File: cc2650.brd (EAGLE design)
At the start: 50.8 x 22.9 mm, 23 parts, among them IC1 TPS73133DBVR, IC4 CC2650MODAMOHR, SW1 SPST_TACT-KMR2, SW3 SPST_TACT-KMR2

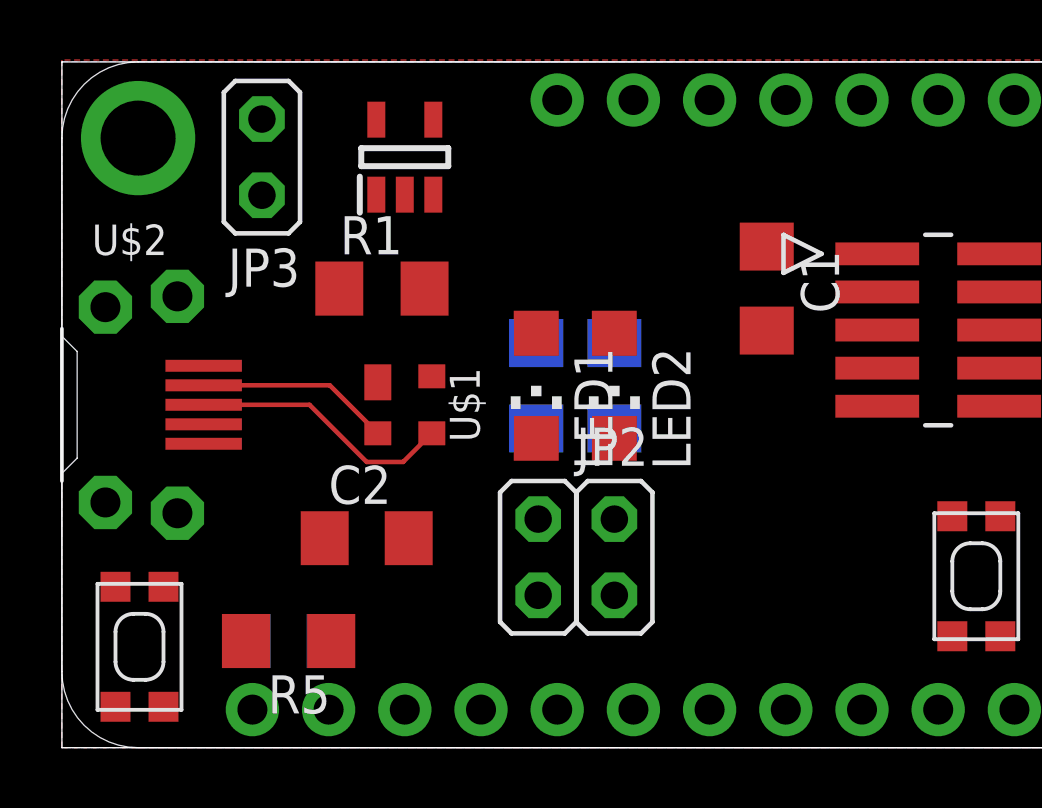
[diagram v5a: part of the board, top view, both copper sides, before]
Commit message: rearranged some components and hand routed some power signals.
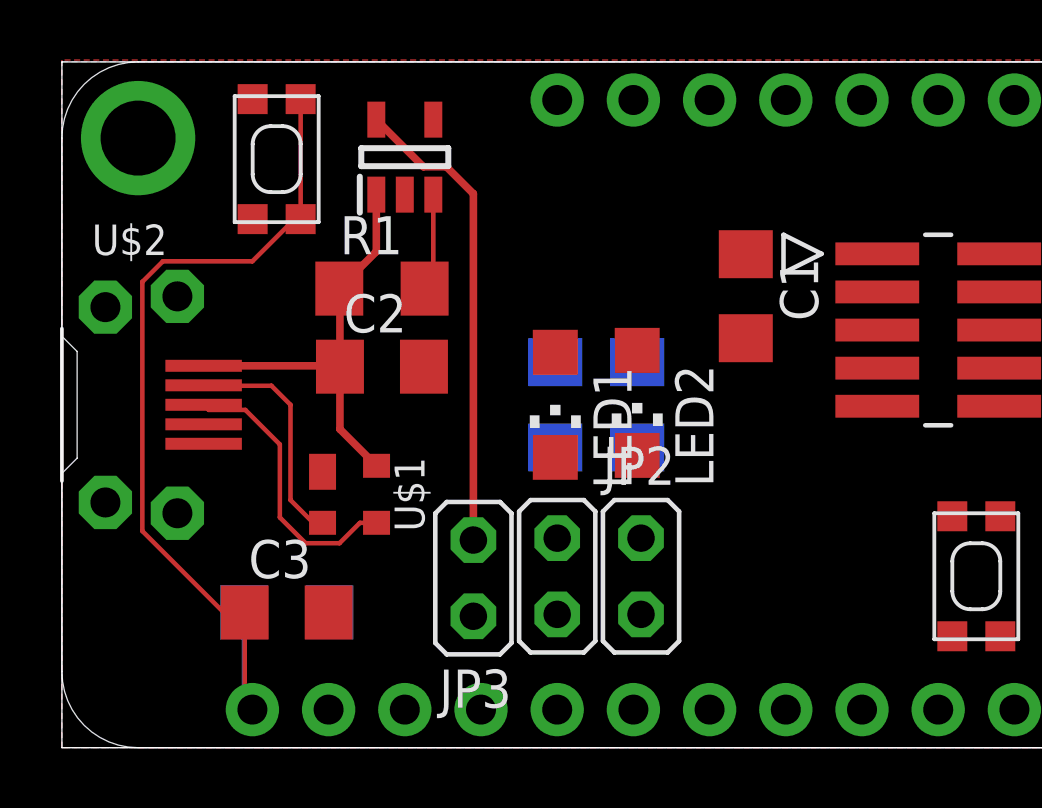
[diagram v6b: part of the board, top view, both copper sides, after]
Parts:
- moved SW1 16.9 mm to (7.16, 19.6)
- moved JP3 15.7 mm to (13.7, 5.65)
- moved C2 5.74 mm to (10.7, 12.7)
- moved U$1 3.51 mm to (9.59, 8.45)
- moved JP2 1.09 mm to (19.3, 5.71)
- moved R2 0.99 mm to (19.2, 11.4)
- moved C3 0.95 mm to (7.49, 4.51), flipped to the top, turned to 0 degrees
- moved R5 0.95 mm to (7.49, 4.51), flipped to the bottom, turned to 0 degrees
- moved LED2 0.95 mm to (19.2, 11.5)
- moved JP1 0.90 mm to (16.5, 5.71)
- moved LED1 0.90 mm to (16.4, 11.4)
- moved R3 0.90 mm to (16.4, 11.4)
- moved C1 0.74 mm to (22.8, 15.0)
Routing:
- net NRESET: track 0.00 -> 30.0 mm
- net N$5: track 0.00 -> 15.8 mm
- net VBUS: track 0.00 -> 14.6 mm
- net EN: track 0.00 -> 3.25 mm
- net D-: track 6.47 -> 7.72 mm
- net D+: track 8.79 -> 9.38 mm

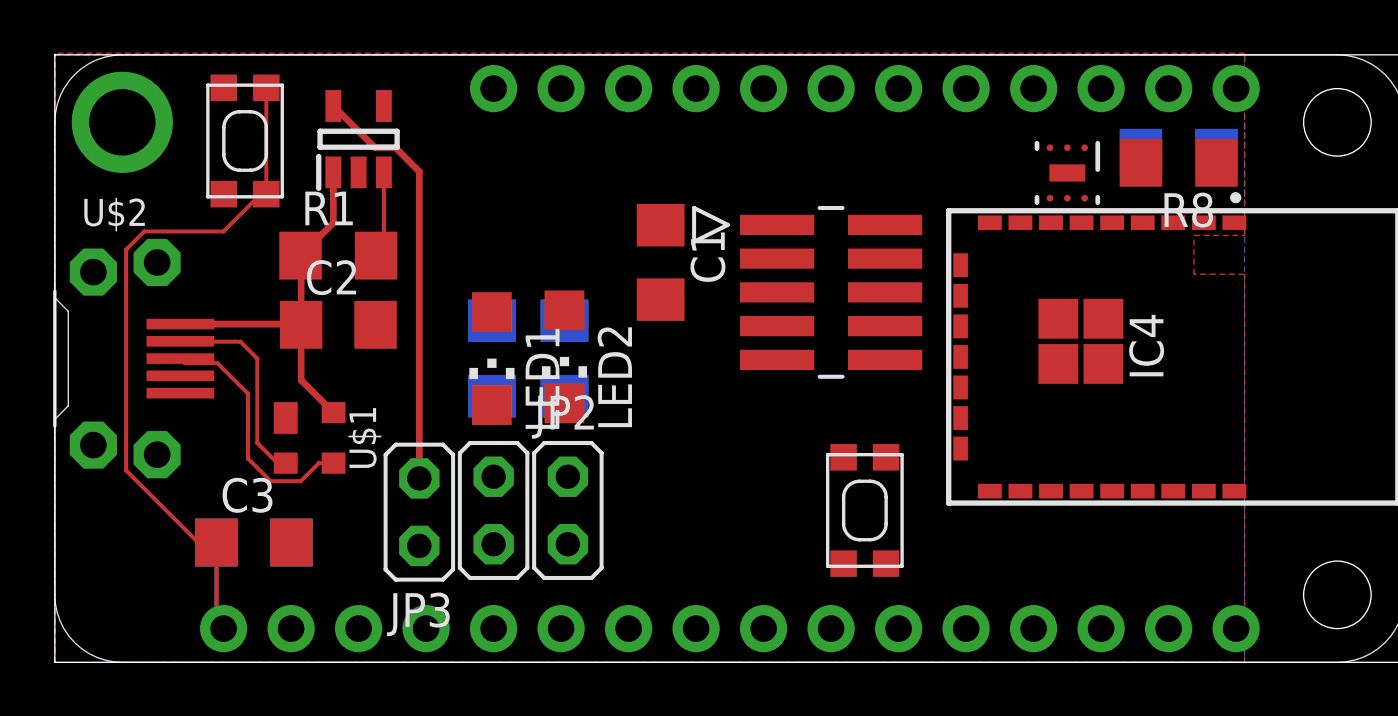
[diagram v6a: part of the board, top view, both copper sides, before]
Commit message: routed everything but light sensor
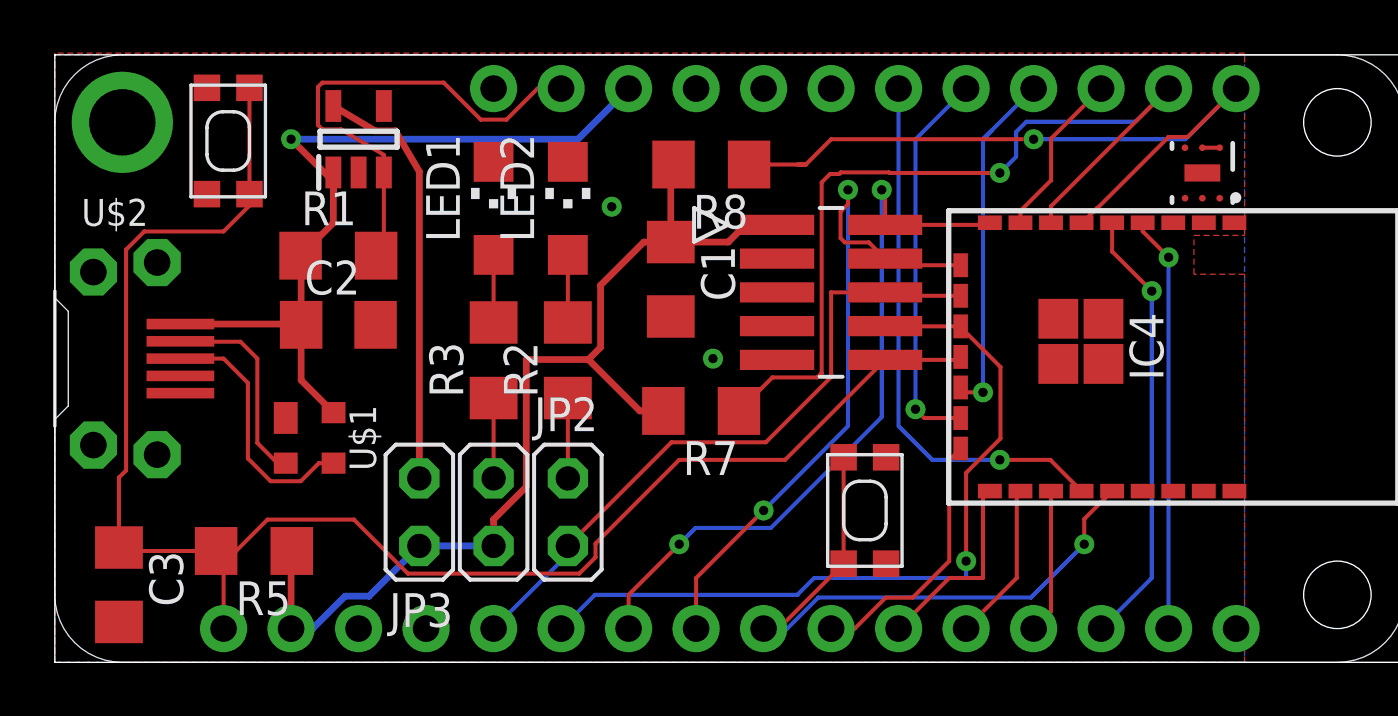
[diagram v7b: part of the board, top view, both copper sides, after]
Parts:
- moved R7 20.4 mm to (24.3, 9.46), flipped to the top, turned to 180 degrees
- moved R8 17.6 mm to (24.7, 18.7)
- moved LED1 5.65 mm to (16.5, 17.1), turned to 0 degrees
- moved LED2 5.59 mm to (19.3, 17.1), turned to 0 degrees
- moved C3 5.32 mm to (2.41, 2.92), turned to 270 degrees
- moved OPT3001 5.08 mm to (43.2, 18.4)
- moved C1 0.74 mm to (23.2, 14.4)
- moved SW1 0.63 mm to (6.52, 19.6)
- moved R5 0.32 mm to (7.49, 4.19), flipped to the top, turned to 180 degrees
- moved R2 0.14 mm to (19.3, 11.4), flipped to the top
- moved R3 0.09 mm to (16.5, 11.4), flipped to the top
- moved JP1 0.06 mm to (16.5, 5.65)
- moved JP2 0.06 mm to (19.3, 5.65)
- turned SW3 to 270 degrees
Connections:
- net N$1 renamed PWR_LED_JPR
- net N$2 renamed GPIO_LED
- net N$3 renamed GPIO_LED_JPR
- net N$32 renamed PWR_LED
- net N$5 renamed VCC_JPR
- removed net VBAT: MS1.28
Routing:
- net VCC: track 0.00 -> 39.5 mm
- net DIO3: track 0.00 -> 32.9 mm, vias 0 -> 1
- net NRESET: track 30.0 -> 62.1 mm
- net DIO6_TDI: track 0.00 -> 29.5 mm, vias 0 -> 1
- net DIO2: track 0.00 -> 27.9 mm, vias 0 -> 1
- net JTAG_TMS: track 0.00 -> 27.5 mm, vias 0 -> 2
- net JTAG_TCK: track 0.00 -> 25.7 mm, vias 0 -> 2
- net DIO5_TDO: track 0.00 -> 24.9 mm
- net DIO14: track 0.00 -> 23.8 mm, vias 0 -> 1
- net DIO13: track 0.00 -> 20.7 mm, vias 0 -> 1
- net DIO1_RX: track 0.00 -> 16.7 mm, vias 0 -> 1
- net VBUS: track 14.6 -> 30.7 mm, vias 0 -> 1
- net DIO0_TX: track 0.00 -> 15.7 mm, vias 0 -> 1
- net EN: track 3.25 -> 18.4 mm
- net DIO8: track 0.00 -> 14.7 mm, vias 0 -> 1
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
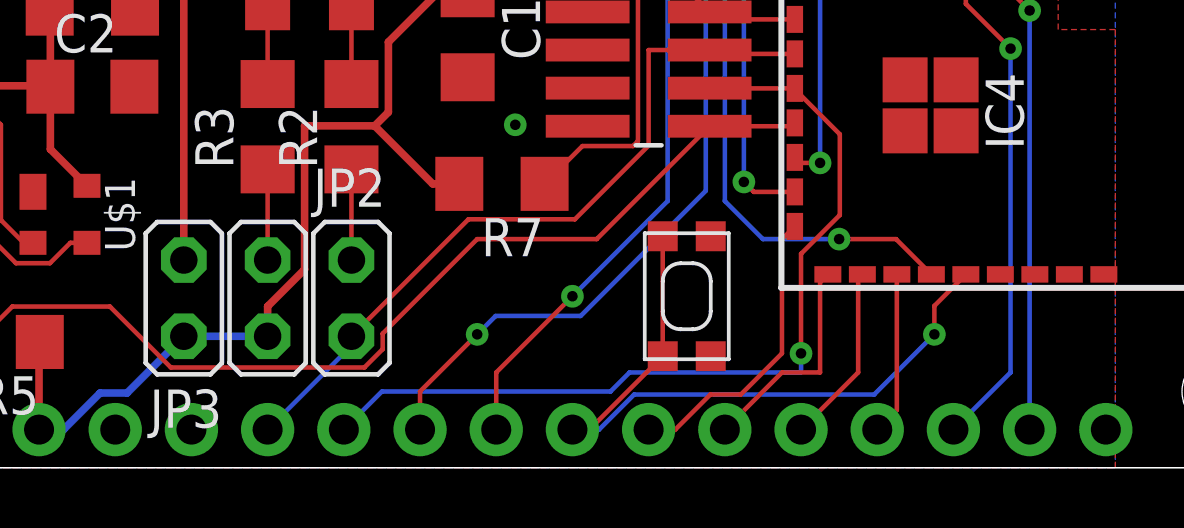
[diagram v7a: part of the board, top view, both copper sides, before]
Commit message: added one missed VCC connection
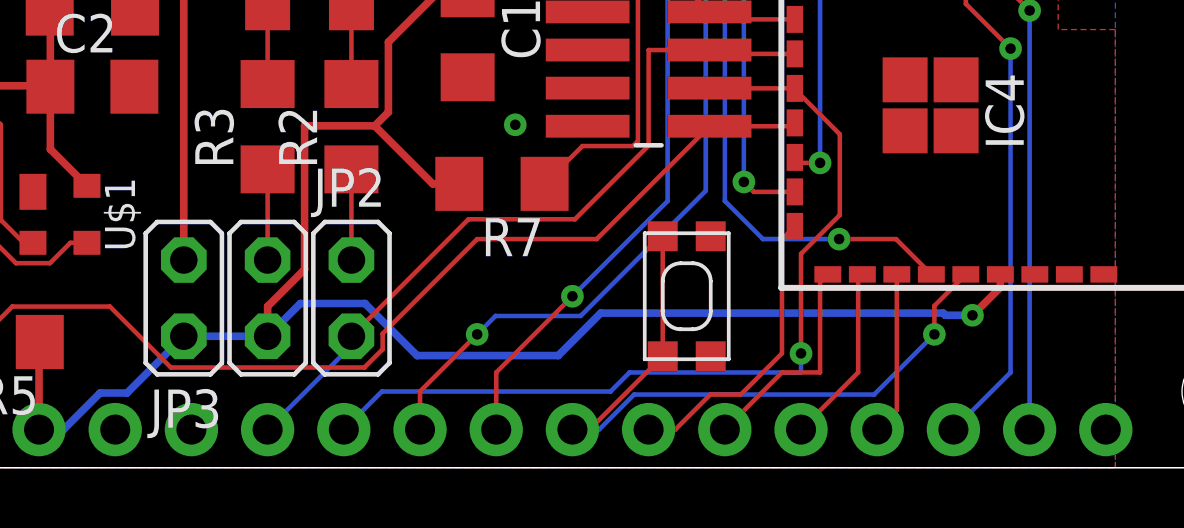
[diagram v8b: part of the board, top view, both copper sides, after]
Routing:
- net VCC: track 39.5 -> 66.6 mm, vias 0 -> 1
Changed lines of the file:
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@@
 <contactref element="MS1" pad="2"/>
 <contactref element="JP3" pad="2"/>
-<wire x1="13.716" y1="4.3815" x2="16.51" y2="4.3815" width="0.254" layer="16"/>
+<wire x1="16.51" y1="4.3815" x2="13.716" y2="4.3815" width="0.254" layer="16"/>
 <wire x1="27.1655" y1="16.4495" x2="27.178" y2="16.462" width="0.1524" layer="1"/>
 <wire x1="8.89" y1="1.27" x2="8.89" y2="4.166" width="0.254" layer="1"/>
@@
 <wire x1="22.011875" y1="9.4615" x2="20.078675" y2="11.3947" width="0.254" layer="1"/>
 <wire x1="43.18" y1="19.365" x2="43.83" y2="19.365" width="0.1524" layer="1"/>
+<wire x1="40.934" y1="6.4435" x2="40.934" y2="6.009" width="0.254" layer="1"/>
+<wire x1="40.934" y1="6.009" x2="40.005" y2="5.08" width="0.254" layer="1"/>
+<via x="40.005" y="5.08" extent="1-16" drill="0.35"/>
+<wire x1="40.005" y1="5.08" x2="39.10183125" y2="5.08" width="0.254" layer="16"/>
+<wire x1="39.10183125" y1="5.08" x2="39.02843125" y2="5.1534" width="0.254" layer="16"/>
+<wire x1="39.02843125" y1="5.1534" x2="27.613125" y2="5.1534" width="0.254" layer="16"/>
+<wire x1="27.613125" y1="5.1534" x2="26.196325" y2="3.7366" width="0.254" layer="16"/>
+<wire x1="26.196325" y1="3.7366" x2="21.49350625" y2="3.7366" width="0.254" layer="16"/>
+<wire x1="21.49350625" y1="3.7366" x2="19.75640625" y2="5.4737" width="0.254" layer="16"/>
+<wire x1="19.75640625" y1="5.4737" x2="17.6022" y2="5.4737" width="0.254" layer="16"/>
+<wire x1="17.6022" y1="5.4737" x2="16.51" y2="4.3815" width="0.254" layer="16"/>
 <wire x1="42.084" y1="6.4435" x2="43.18" y2="19.365" width="0" layer="19" extent="1-1"/>
 <wire x1="40.934" y1="6.4435" x2="42.084" y2="6.4435" width="0" layer="19" extent="1-1"/>
-<wire x1="27.178" y1="16.462" x2="43.18" y2="19.365" width="0" layer="19" extent="1-1"/>
 </signal>
 <signal name="VBUS" class="2">
